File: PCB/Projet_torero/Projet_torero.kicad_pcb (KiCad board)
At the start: 4 copper layers, 54 x 57 mm, 75 parts, among them IC501 MP1475SGJ-P, J201 Conn_02x07_Odd_Even, J202 Conn_02x08_Odd_Even, J401 Conn_01x08, J501 Conn_01x02, J502 Conn_01x02, J601 Conn_01x06, J701 Conn_01x06, SW201 SW_Push, SW202 SW_Push, U201 STM32G431CBUx, U401 ADXL343, U501 BU33SD5WG-TR, U601 ZXBM5210-SP, U701 ZXBM5210-SP, Y201 Crystal_GND24_Small

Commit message: routage à valider
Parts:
- moved C207 0.70 mm to (177.3, 75.5)
- moved C209 0.70 mm to (177.9, 76.8)
- moved C204 0.56 mm to (171.3, 84.8)
- moved C210 0.43 mm to (171.8, 87.3)
- moved C211 0.34 mm to (172.3, 84.0)
- moved C205 0.30 mm to (169.4, 86.5)
- moved C208 0.23 mm to (173.7, 84.3)
- moved R205 0.07 mm to (151.9, 96.5)
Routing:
- net NRST: track 0.00 -> 73.3 mm, vias 0 -> 4
- net LED_N: track 0.00 -> 69.8 mm, vias 0 -> 4
- net /STM32/USER_BTN: track 0.00 -> 68.6 mm, vias 0 -> 6
- net GND: track 0.00 -> 65.3 mm, vias 25 -> 70
- net VCP_RX: track 0.00 -> 57.8 mm, vias 0 -> 2
- net LED_E: track 0.00 -> 51.0 mm, vias 0 -> 2
- net /CAPTEURS/DEV_EN_LIDAR: track 0.00 -> 47.9 mm, vias 0 -> 1
- net /CAPTEURS/ANALOG_OUTPUT_CAPT_BORD_D: track 0.00 -> 46.9 mm, vias 0 -> 2
- net /CAPTEURS/INT2_ACC: track 0.00 -> 45.8 mm, vias 0 -> 2
- net LED_W: track 0.00 -> 45.5 mm, vias 0 -> 2
- net Net-(U201-VBAT): track 0.50 -> 45.8 mm, vias 0 -> 4
- net VCP_TX: track 0.00 -> 44.1 mm, vias 0 -> 2
- net /PUISSANCE/EncodeurB_Droite: track 0.00 -> 42.4 mm, vias 0 -> 2
- net /PUISSANCE/EncodeurA_Droite: track 0.00 -> 40.4 mm, vias 0 -> 2
- net /CAPTEURS/Tx_LIDAR: track 0.00 -> 40.3 mm
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- added copper zone on In2.Cu, net +5V

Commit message: Correction du PCB pour prof
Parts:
- moved R204 0.39 mm to (150.4, 96.4)
- moved R209 0.25 mm to (157.9, 96.5)
- moved R210 0.23 mm to (159.4, 96.5)
- moved R211 0.23 mm to (160.9, 96.5)
- moved R208 0.13 mm to (156.4, 96.5)
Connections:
- R802 pad 2: +5V -> +3.3V
- R902 pad 2: +5V -> +3.3V
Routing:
- net Net-(J601-Pin_1): track 20.0 -> 16.7 mm, vias 0 -> 2
- net +5V: track 9.14 -> 6.28 mm, vias 8 -> 6
- net +3.3V: track 30.1 -> 33.0 mm, vias 16 -> 18
- net Net-(J701-Pin_1): track 9.44 -> 11.5 mm
- net Net-(U201-VBAT): track 45.8 -> 43.8 mm
- net Net-(J701-Pin_6): track 28.3 -> 30.2 mm
- net STATUS_LED: track 7.31 -> 5.56 mm
- net VCP_RX: track 57.8 -> 56.3 mm
- net /CAPTEURS/INT2_ACC: track 45.8 -> 44.4 mm
- net LED_E: track 51.0 -> 49.7 mm
- net SWCLK: track 17.8 -> 18.7 mm
- net /PUISSANCE/REVG: track 26.1 -> 26.9 mm
- net SWO: track 21.3 -> 22.1 mm
- net SWDIO: track 16.5 -> 17.3 mm
- net /CAPTEURS/M_EN_LIDAR: track 34.1 -> 33.4 mm
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
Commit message: Correction suggestion prof
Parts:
- moved C204 11.2 mm to (165.9, 75.0), turned to 180 degrees
- moved C601 2.38 mm to (170.4, 63.0)
- moved U601 2.38 mm to (174.8, 61.6)
- moved C602 2.38 mm to (170.4, 59.9)
- moved C702 0.94 mm to (157.9, 59.9)
- moved U701 0.94 mm to (162.3, 61.6)
- moved C701 0.94 mm to (157.9, 63.0)
- moved C703 0.69 mm to (155.4, 56.1)
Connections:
- net Net-(IC501-SW) renamed /ALIMENTATION/Sortie Régulateur 5V
- J601 pad 1: Net-(J601-Pin_1) -> /PUISSANCE/Moteur/Commande moteur
- J601 pad 6: Net-(J601-Pin_6) -> /PUISSANCE/Moteur/Connecteur Moteur
- J701 pad 1: Net-(J701-Pin_1) -> /PUISSANCE/Moteur1/Commande moteur
- J701 pad 6: Net-(J701-Pin_6) -> /PUISSANCE/Moteur1/Connecteur Moteur
- U601 pad 1: Net-(J601-Pin_1) -> /PUISSANCE/Moteur/Connecteur Moteur
- U601 pad 7: Net-(J601-Pin_6) -> /PUISSANCE/Moteur/Commande moteur
- U701 pad 1: Net-(J701-Pin_1) -> /PUISSANCE/Moteur1/Connecteur Moteur
- U701 pad 7: Net-(J701-Pin_6) -> /PUISSANCE/Moteur1/Commande moteur
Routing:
- net Net-(J701-Pin_6): track 30.2 -> 0.00 mm, vias 2 -> 0
- net Net-(J601-Pin_6): track 18.8 -> 0.00 mm
- net Net-(J601-Pin_1): track 16.7 -> 0.00 mm, vias 2 -> 0
- net /ALIMENTATION/Sortie Régulateur 5V: track 12.5 -> 0.00 mm
- net Net-(J701-Pin_1): track 11.5 -> 0.00 mm, vias 2 -> 0
- net GND: track 65.3 -> 70.0 mm, vias 69 -> 70
- net /PUISSANCE/EncodeurA_Droite: track 40.4 -> 44.9 mm, vias 2 -> 3
- net +5V: track 6.28 -> 9.78 mm, vias 6 -> 8
- net /PUISSANCE/FWDG: track 27.0 -> 29.2 mm
- net +3.3V: track 33.0 -> 31.2 mm
- net 7.2V: track 18.0 -> 16.2 mm
- net /PUISSANCE/REVG: track 26.9 -> 28.4 mm
- net /PUISSANCE/Moteur/Connecteur Moteur: track 0.00 -> 0.91 mm
- net /PUISSANCE/Moteur/Commande moteur: track 0.00 -> 0.57 mm
- net /PUISSANCE/EncodeurB_Droite: track 42.3 -> 42.6 mm, vias 2 -> 3
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- added copper zone on B.Cu, net /ALIMENTATION/Sortie Régulateur 5V
- added copper zone on F.Cu, net /ALIMENTATION/Sortie Régulateur 5V
- added copper zone on F.Cu, net /PUISSANCE/Moteur/Commande moteur
- added copper zone on F.Cu, net /PUISSANCE/Moteur/Connecteur Moteur
- added copper zone on F.Cu, net /PUISSANCE/Moteur1/Commande moteur
- added copper zone on F.Cu, net /PUISSANCE/Moteur1/Connecteur Moteur

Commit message: Confirmation PCB
Il manque juste a finir le texte et mettre les logos de l'ENSEA et du groupe TORERO
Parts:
- added TP1: TestPoint, TestPoint:TestPoint_Pad_D1.5mm, F.Cu at (173.9, 65.5)
- added TP2: TestPoint, TestPoint:TestPoint_Pad_D1.5mm, F.Cu at (161.5, 66.0)
- added TP3: TestPoint, TestPoint:TestPoint_Pad_D1.5mm, F.Cu at (177.4, 66.2)
- added TP4: TestPoint, TestPoint:TestPoint_Pad_D1.5mm, F.Cu at (165.3, 65.5)
- Hacheur D: renamed from U601
- LEDs Lidar: renamed from J202
- Moteur D: renamed from J601
- Moteur G: renamed from J701
- renumbered U401 to Acc, J501 to Batterie, QRD901 to CapteurBD, QRD801 to CapteurBG, U701 to HacheurG, J401 to LIDAR, J502 to ON/OFF, SW202 to Reset, U501 to Régu3.3V, IC501 to Régu5V, J201 to ST-LINK
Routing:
- net GND: track 70.0 -> 57.1 mm, vias 70 -> 69
- net +3.3V: track 31.2 -> 27.1 mm
- net /PUISSANCE/FWDD: track 24.7 -> 27.3 mm
- net NRST: track 73.2 -> 74.7 mm
- net VCP_TX: track 44.1 -> 43.0 mm
- net /PUISSANCE/REVD: track 17.4 -> 18.4 mm
- net /PUISSANCE/Moteur/Connecteur Moteur: track 0.91 -> 0.00 mm
- net LED_N: track 69.3 -> 70.0 mm
- net LED_NW: track 27.8 -> 28.4 mm
- net 7.2V: track 16.2 -> 15.7 mm
- removed copper zone on B.Cu, net /ALIMENTATION/Sortie Régulateur 5V
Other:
- board text added: "+"
- board text added: "-"
- board text added: "Projet Torero"
- board text added: "User BTN"

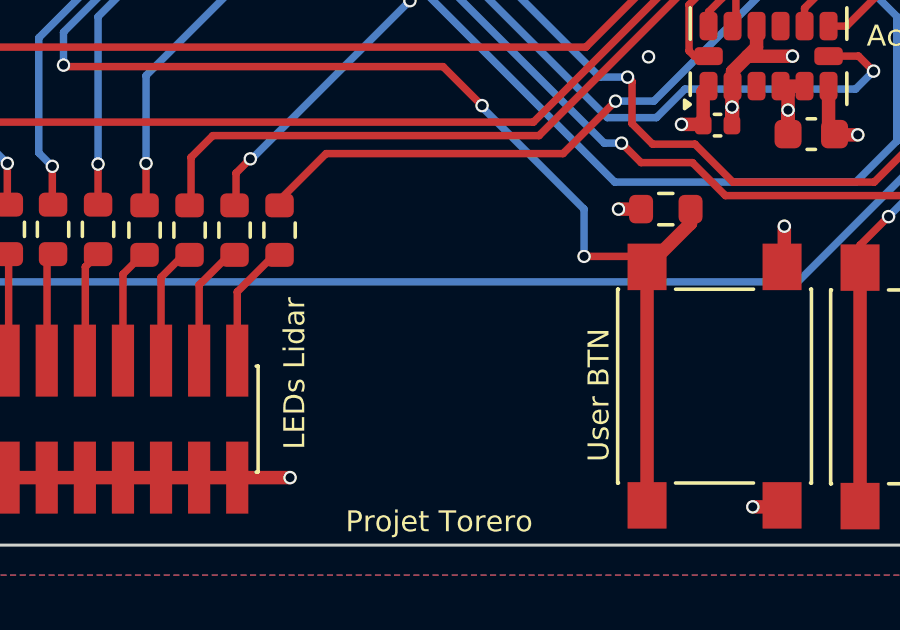
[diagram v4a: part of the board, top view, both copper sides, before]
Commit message: fichier gerber et ajout logo ensea
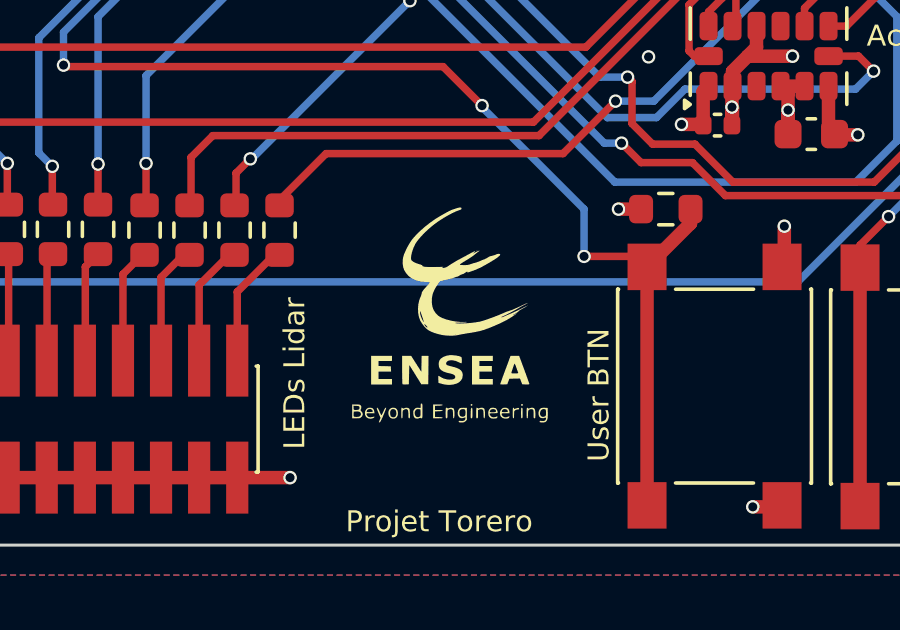
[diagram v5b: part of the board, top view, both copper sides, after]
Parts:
- added G***: LOGO, Graphic:logo_Ensea, F.Cu at (166.6, 99.3)

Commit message: ajout cornes taureau
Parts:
- added G***: LOGO, Graphic:logo_taureau, F.Cu at (153.8, 87.3)
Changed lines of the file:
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@@
+		)
+	)
+	(footprint "Graphic:logo_taureau"
+		(layer "F.Cu")
+		(at 153.775 87.35)
+		(property "Reference" "G***"
+			(at 0 0 0)
+			(layer "F.SilkS")
+			(hide yes)
+			(effects
+				(font
+					(size 1.5 1.5)
+					(thickness 0.3)
+				)
+			)
+		)
+		(property "Value" "LOGO"
+			(at 0.75 0 0)
+			(layer "F.SilkS")
+			(hide yes)
+			(effects
+				(font
+					(size 1.5 1.5)
+					(thickness 0.3)
+				)
+			)
+		)
+		(property "Footprint" "Graphic:logo_taureau"
+			(at 0 0 0)
+			(layer "F.Fab")
+			(hide yes)
+			(effects
+				(font
+					(size 1.27 1.27)
+					(thickness 0.15)
+				)
+			)
+		)
+		(property "Datasheet" ""
+			(at 0 0 0)
+			(layer "F.Fab")
+			(hide yes)
+			(effects
+				(font
+					(size 1.27 1.27)
+					(thickness 0.15)
+				)
+			)
+		)
+		(property "Description" ""
+			(at 0 0 0)
+			(layer "F.Fab")
+			(hide yes)
+			(effects
+				(font
+					(size 1.27 1.27)
+					(thickness 0.15)
+				)
+			)
+		)
+		(attr board_only exclude_from_pos_files exclude_from_bom)
+		(fp_poly
+			(pts
+				(xy -2.426657 -1.702323) (xy -2.387647 -1.639302) (xy -2.330647 -1.542716) (xy -2.260683 -1.421014)
+				(xy -2.219939 -1.348993) (xy -2.004948 -0.966931) (xy -1.202256 -0.9525) (xy -0.399563 -0.938068)
+				(xy -0.300805 -0.830253) (xy -0.202046 -0.722438) (xy -0.202046 0.374804) (xy -0.202594 0.619977)
+				(xy -0.204158 0.845979) (xy -0.206613 1.046555) (xy -0.209835 1.215451) (xy -0.213702 1.346415)
+				(xy -0.21809 1.433191) (xy -0.222874 1.469528) (xy -0.223693 1.470241) (xy -0.251942 1.45128) (xy -0.314395 1.400531)
+				(xy -0.402609 1.325113) (xy -0.508139 1.232142) (xy -0.540399 1.203253) (xy -0.835458 0.938069)
+				(xy -0.836252 0.223694) (xy -0.837046 -0.490681) (xy -1.435966 -0.490789) (xy -1.63954 -0.49126)
+				(xy -1.793902 -0.493051) (xy -1.907562 -0.496857) (xy -1.989033 -0.503372) (xy -2.046826 -0.513288)
+				(xy -2.089451 -0.527301) (xy -2.125422 -0.546105) (xy -2.127125 -0.547139) (xy -2.201825 -0.603732)
+				(xy -2.258807 -0.665328) (xy -2.261716 -0.669701) (xy -2.276037 -0.711961) (xy -2.296273 -0.797753)
+				(xy -2.320521 -0.916009) (xy -2.346882 -1.055658) (xy -2.373454 -1.205633) (xy -2.398337 -1.354862)
+				(xy -2.419629 -1.492278) (xy -2.435431 -1.606812) (xy -2.44384 -1.687393) (xy -2.442956 -1.722953)
+				(xy -2.442652 -1.723333)
+			)
+			(stroke
+				(width 0)
+				(type solid)
+			)
+			(fill solid)
+			(layer "F.SilkS")
+		)
+		(fp_poly
+			(pts
+				(xy 2.325771 -1.691167) (xy 2.317689 -1.611926) (xy 2.302247 -1.498469) (xy 2.281344 -1.362009)
+				(xy 2.256881 -1.213757) (xy 2.230756 -1.064924) (xy 2.204869 -0.926722) (xy 2.18112 -0.810363) (xy 2.161408 -0.727058)
+				(xy 2.149403 -0.690914) (xy 2.092352 -0.614774) (xy 2.015926 -0.54979) (xy 2.011837 -0.54724) (xy 1.975947 -0.528158)
+				(xy 1.933878 -0.513907) (xy 1.877115 -0.503793) (xy 1.797143 -0.497119) (xy 1.685448 -0.493192)
+				(xy 1.533515 -0.491314) (xy 1.33283 -0.490793) (xy 1.320511 -0.490789) (xy 0.721591 -0.490681) (xy 0.721149 0.209262)
+				(xy 0.720183 0.405417) (xy 0.717706 0.582773) (xy 0.713965 0.733038) (xy 0.709204 0.847921) (xy 0.703671 0.919132)
+				(xy 0.699501 0.938513) (xy 0.669707 0.969728) (xy 0.608204 1.028001) (xy 0.524654 1.10472) (xy 0.428718 1.191268)
+				(xy 0.330059 1.279034) (xy 0.238338 1.359402) (xy 0.163216 1.423758) (xy 0.114357 1.46349) (xy 0.10107 1.472046)
+				(xy 0.097833 1.444227) (xy 0.094849 1.364948) (xy 0.092199 1.240478) (xy 0.089967 1.077082) (xy 0.088234 0.88103)
+				(xy 0.087085 0.658588) (xy 0.086601 0.416023) (xy 0.086591 0.374804) (xy 0.086591 -0.722438) (xy 0.185349 -0.830253)
+				(xy 0.284108 -0.938068) (xy 1.084772 -0.9525) (xy 1.885435 -0.966931) (xy 2.101694 -1.349755) (xy 2.176764 -1.481449)
+				(xy 2.241399 -1.592569) (xy 2.290593 -1.674688) (xy 2.319339 -1.719377) (xy 2.324594 -1.724982)
+			)
+			(stroke
+				(width 0)
+				(type solid)
+			)
+			(fill solid)
+			(layer "F.SilkS")
 		)
 	)

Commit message: Add files via upload
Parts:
- added G***: LOGO, Graphic:Logo_Niko, F.Cu at (151.0, 63.5)
